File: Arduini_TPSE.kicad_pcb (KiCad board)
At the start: 2 copper layers, 26 x 57.5 mm, 25 parts, among them J1 2134441-2, J2 ICSP, P1 Digital, P2 Analog, SW1 SW_Push, U1 AMS1117-3.3, U2 FT232RL, U3 ATmega328-P, U4 AMS1117-5.0, Y1 16Mhz

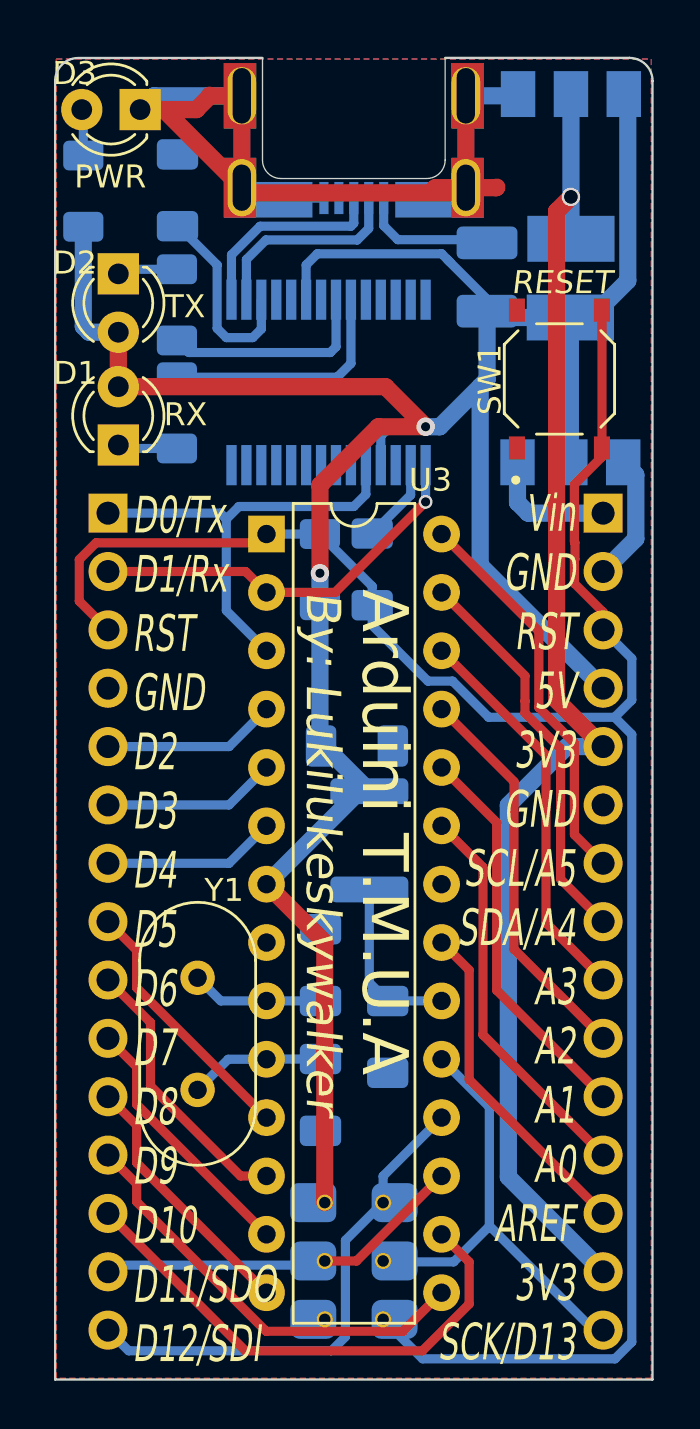
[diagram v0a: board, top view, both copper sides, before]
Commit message: Condensadores 3V3, 5V, y recolocacion
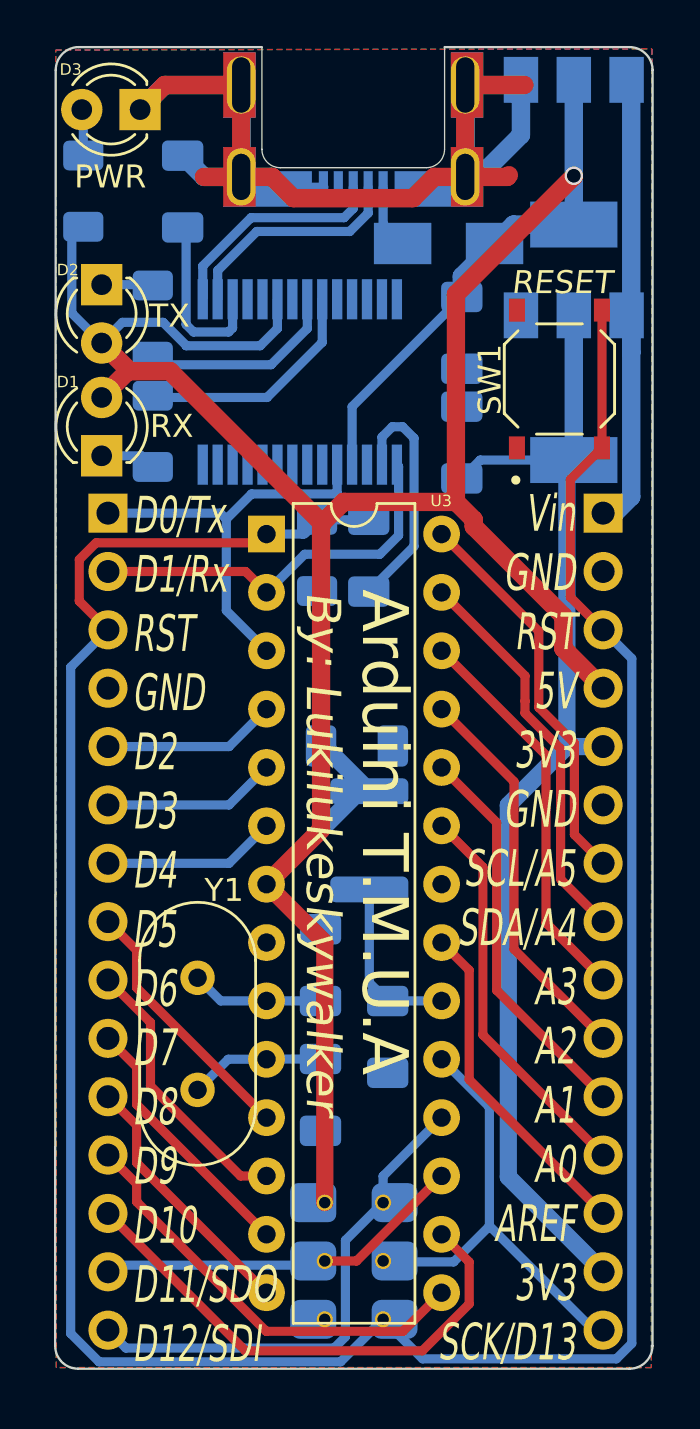
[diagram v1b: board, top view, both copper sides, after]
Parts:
- added C7: 100u, Capacitor_SMD:C_1206_3216Metric_Pad1.33x1.80mm_HandSolder, B.Cu at (141.3, 47.7)
- added C8: 100u, Capacitor_SMD:C_1206_3216Metric_Pad1.33x1.80mm_HandSolder, B.Cu at (141.3, 52.5)
- D4: footprint Diode_SMD:D_1210_3225Metric_Pad1.42x2.65mm_HandSolder -> Diode_SMD:D_SMA
- moved U1 10.3 mm to (146.2, 39.9), turned to -90 degrees
- moved U4 9.63 mm to (146.2, 50.1)
- moved D4 2.22 mm to (140.8, 43.8), turned to 180 degrees
- moved R1 1.32 mm to (127.9, 52.0)
- moved R2 1.26 mm to (127.9, 47.2)
- moved U2 1.25 mm to (134.3, 49.9)
- moved D1 0.86 mm to (125.7, 53.1)
- moved D2 0.86 mm to (125.7, 45.6)
- moved R3 0.63 mm to (135.0, 57.4)
- moved C1 0.61 mm to (137.3, 57.4), turned to 90 degrees
- moved J1 0.47 mm to (136.6, 36.9)
- moved C6 0.23 mm to (129.2, 41.6)
- renumbered U4 to U1, U1 to U4
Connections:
- U4 pad 3: +5V -> /Vin
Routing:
- net /Reset: track 91.0 -> 122.4 mm
- net /Vin: track 5.67 -> 21.7 mm
- net +5V: track 122.8 -> 133.8 mm, vias 2 -> 1
- net GND: track 47.7 -> 58.2 mm
- net +3V3: track 58.5 -> 51.3 mm, vias 1 -> 0
- net Net-(C1-Pad1): track 4.15 -> 10.5 mm
- net Net-(D4-Pad2): track 5.53 -> 2.80 mm
- net /1(Tx): track 19.5 -> 18.3 mm
- net /D+: track 8.94 -> 9.96 mm
- net /D-: track 8.96 -> 9.96 mm
- net /3V3OUT: track 8.71 -> 7.77 mm
- net Net-(R2-Pad1): track 9.30 -> 8.65 mm
- net Net-(D2-Pad1): track 2.63 -> 2.02 mm
- net /0(Rx): track 17.4 -> 17.2 mm, vias 1 -> 0
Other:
- outline, holes or cut-outs redrawn
- board text added: "AMS1117 3V3"
- board text added: "AMS1117 5V"
- board text removed: "LT1117 3V3"
- board text removed: "LT1117 5V"

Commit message: Ampliacion
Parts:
- removed the D4 at (140.8, 43.8)
- added C10: 100n, Capacitor_SMD:C_1206_3216Metric_Pad1.33x1.80mm_HandSolder, B.Cu at (18.6, -49.9)
- added C8: 100n, Capacitor_SMD:C_1206_3216Metric_Pad1.33x1.80mm_HandSolder, B.Cu at (23.5, -49.9)
- added D1: D_Schottky, Diode_SMD:D_SMA, B.Cu at (11.7, -49.5)
- C7: footprint Capacitor_SMD:C_1206_3216Metric_Pad1.33x1.80mm_HandSolder -> Capacitor_Tantalum_SMD:CP_EIA-3528-15_AVX-H_Pad1.50x2.35mm_HandSolder
- C9: renamed from C8; footprint Capacitor_SMD:C_1206_3216Metric_Pad1.33x1.80mm_HandSolder -> Capacitor_Tantalum_SMD:CP_EIA-3528-15_AVX-H_Pad1.50x2.35mm_HandSolder
- moved U2 162.6 mm to (22.6, -55.5)
- moved C6 157.9 mm to (3.62, -54.2)
- moved C9 157.7 mm to (17.7, -45.4)
- moved D4 156.4 mm to (3.70, -57.8)
- moved R4 156.4 mm to (1.23, -54.2)
- moved J1 156.1 mm to (13.0, -58.4)
- moved R1 154.7 mm to (4.25, -41.0)
- moved R2 154.7 mm to (4.25, -45.8)
- moved C4 154.6 mm to (11.6, -17.6)
- moved C5 154.6 mm to (11.6, -11.9)
- moved L1 154.6 mm to (13.7, -23.0)
- moved C1 154.6 mm to (13.7, -35.4)
- moved C2 154.6 mm to (14.5, -14.4)
- moved C3 154.6 mm to (13.1, -27.1)
- moved D2 154.6 mm to (2.02, -47.2)
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- renumbered D1 to D3, D3 to D4, U4 to U2, U2 to U3, U3 to U4
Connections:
- P2 pad 5: +3V3 -> GND
- P2 pad 6: GND -> +3V3
- U2 pad 3: /Vin -> +5V
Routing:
- net +5V: track 133.8 -> 152.9 mm, vias 1 -> 0
- net +3V3: track 51.3 -> 65.4 mm
- net GND: track 58.2 -> 44.9 mm
- net /Vin: track 21.7 -> 9.50 mm
- net /3V3OUT: track 7.77 -> 11.3 mm
- net /D+: track 9.96 -> 12.5 mm
- net /D-: track 9.96 -> 12.5 mm
- net Net-(J1-Pad1): track 2.80 -> 4.64 mm
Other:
- board size 26 x 57.5 mm -> 26 x 60 mm

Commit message: Version presentada
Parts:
- added G***: LOGO, Badges:wokeupforthis, F.Cu at (12.9, -45.6)
- moved C9 0.61 mm to (17.7, -46.0)
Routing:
- net /Reset: track 122.4 -> 172.8 mm
- net +5V: track 152.9 -> 154.6 mm
- net +3V3: track 65.4 -> 64.1 mm
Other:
- board text added: "Vin GND RST 5V GND 3V3 A5/SCL A4/SDA A3 A2 A1 A0 AREF 3V3 D13/SCK"
- board text added: "Vin GND RST 5V GND 3V3 SCL/A5 SDA/A4 A3 A2 A1 A0 AREF 3V3 SCK/D13"
- board text removed: "Vin GND RST 5V 3V3 GND A5/SCL A4/SDA A3 A2 A1 A0 AREF 3V3 D13/SCK"
- board text removed: "Vin GND RST 5V 3V3 GND SCL/A5 SDA/A4 A3 A2 A1 A0 AREF 3V3 SCK/D13"
